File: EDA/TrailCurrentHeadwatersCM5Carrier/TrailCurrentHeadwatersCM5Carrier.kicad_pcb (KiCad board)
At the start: 4 copper layers, 160 x 90 mm, 79 parts, among them J10 690-019-298-412, J11 USB_C_Receptacle_USB2.0, J12 USB3_A, J14 JST_SHBM04B-SRSS-TB, J16 Conn_01x22_Female, J2 Conn_02x07_Odd_Even, J22 690-019-298-412, J3 Conn_01x03, J4 Bus_M.2_Socket_M, J5 Conn_01x22_Female, J6 THD-02-R, J7 Micro_SD_Card_Det, J8 THD-20-R, J9 THD-02-R, SW1 Right angle Tact button, U1 TPD4EUSB30, U12 RT9742SNGV, U18 RT9742GGJ5, U2 TPD4EUSB30, U3 MagJack-A70-112-331N126, U6 AP22653W6, U7 ASEK-32.768KHZ-L-R-T, U8 AP3441SHE-7B

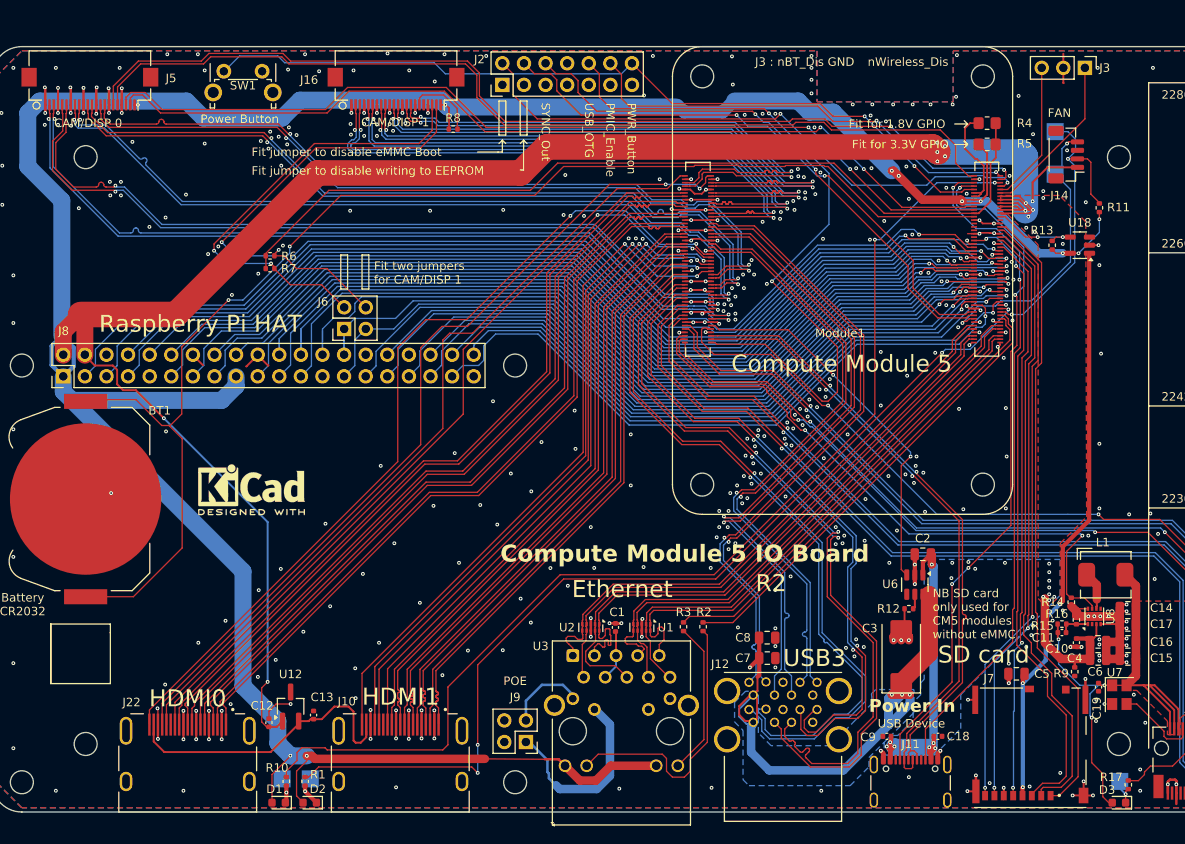
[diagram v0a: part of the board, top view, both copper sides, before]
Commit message: Carrier board updated to point to items brought into our own libraries
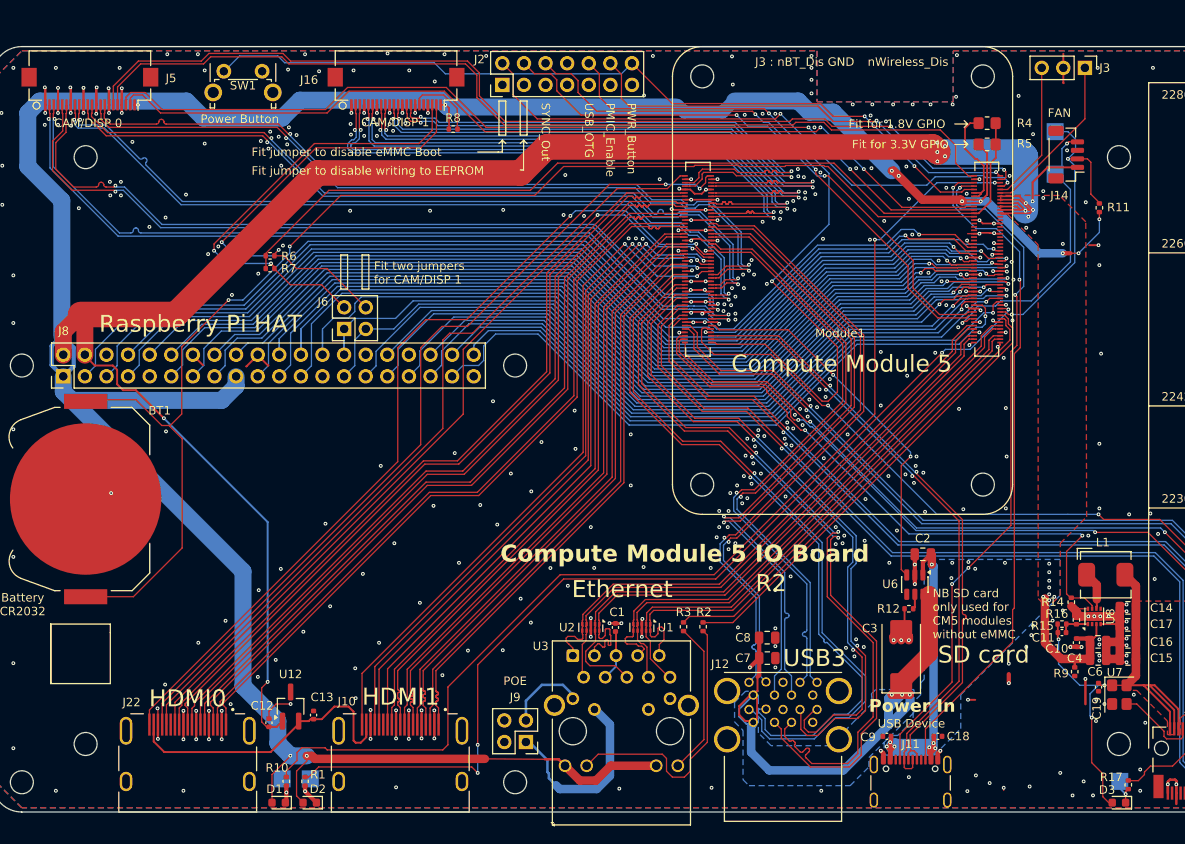
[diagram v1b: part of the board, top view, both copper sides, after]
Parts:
- removed C5: 10u, Capacitor_SMD:C_0805_2012Metric
- removed J7: Micro_SD_Card_Det, TrailCurrentHeadwatersCM5Carrier:SDCARD_MOLEX_503398-1892
- removed R13: 10K 1%, Resistor_SMD:R_0402_1005Metric
- removed REF**: KiCad-Logo2_5mm_SilkScreen, Symbol:KiCad-Logo2_5mm_SilkScreen
- removed U18: RT9742GGJ5, Package_TO_SOT_SMD:SOT-23-5
- BT1: footprint TrailCurrentHeadwatersCM5Carrier:BatteryHolder_Keystone_3034_1x20mm -> TrailCurrentFootprints:BatteryHolder_Keystone_3034_1x20mm
- H1, H2, H3, H4, H5, H6, H7, H8: footprint TrailCurrentHeadwatersCM5Carrier:MountingHole_2.7mm_M2.5_DIN965 -> TrailCurrentFootprints:MountingHole_2.7mm_M2.5_DIN965
- J10, J22: footprint TrailCurrentHeadwatersCM5Carrier:EDAC 690-019-298-412 -> TrailCurrentFootprints:EDAC 690-019-298-412
- J12: footprint TrailCurrentHeadwatersCM5Carrier:MTCONN_UBAF30-D2011 -> TrailCurrentFootprints:MTCONN_UBAF30-D2011
- J16, J5: footprint TrailCurrentHeadwatersCM5Carrier:Hirose_FH12-22S-0.5SH_1x22-1MP_P0.50mm_Horizontal -> TrailCurrentFootprints:Hirose_FH12-22S-0.5SH_1x22-1MP_P0.50mm_Horizontal
- J4: footprint TrailCurrentHeadwatersCM5Carrier:M.2 M Key socket -> TrailCurrentFootprints:M.2 M Key socket
- L1: footprint TrailCurrentHeadwatersCM5Carrier:L_Bourns_SRP5030CC -> TrailCurrentFootprints:L_Bourns_SRP5030CC
- Module1: footprint TrailCurrentHeadwatersCM5Carrier:Raspberry-Pi-5-Compute-Module -> TrailCurrentFootprints:Raspberry-Pi-5-Compute-Module
- U3: footprint TrailCurrentHeadwatersCM5Carrier:TRJG0926HENL -> TrailCurrentFootprints:TRJG0926HENL
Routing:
- net /TrailCurrentHeadwatersCM5Carrier_GPIO/SD_CMD: track 75.2 -> 0.00 mm, vias 2 -> 0
- net /TrailCurrentHeadwatersCM5Carrier_GPIO/SD_DAT2: track 73.6 -> 0.00 mm
- net /TrailCurrentHeadwatersCM5Carrier_GPIO/SD_DAT3: track 72.5 -> 0.00 mm
- net /TrailCurrentHeadwatersCM5Carrier_GPIO/SD_DAT1: track 71.3 -> 0.00 mm, vias 2 -> 0
- net /TrailCurrentHeadwatersCM5Carrier_GPIO/SD_DAT0: track 69.8 -> 0.00 mm, vias 2 -> 0
- net /TrailCurrentHeadwatersCM5Carrier_GPIO/SD_PWR: track 67.9 -> 0.00 mm, vias 3 -> 0
- net /TrailCurrentHeadwatersCM5Carrier_GPIO/SD_CLK: track 67.0 -> 0.00 mm, vias 2 -> 0
- net /TrailCurrentHeadwatersCM5Carrier_GPIO/SD_PWR_ON: track 10.7 -> 0.00 mm, vias 2 -> 0
- net GND: track 764.8 -> 755.4 mm
- net /+3.3v: track 331.7 -> 330.2 mm

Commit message: Working through warnings to cleanup schematic
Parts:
- moved J6 0.60 mm to (120.4, 102.6)
